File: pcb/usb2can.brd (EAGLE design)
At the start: 160 x 100 mm, 18 parts, among them IC1 ADM3053M, IC2 LD117AS33TR, K1 61400416021, K2 61900419521

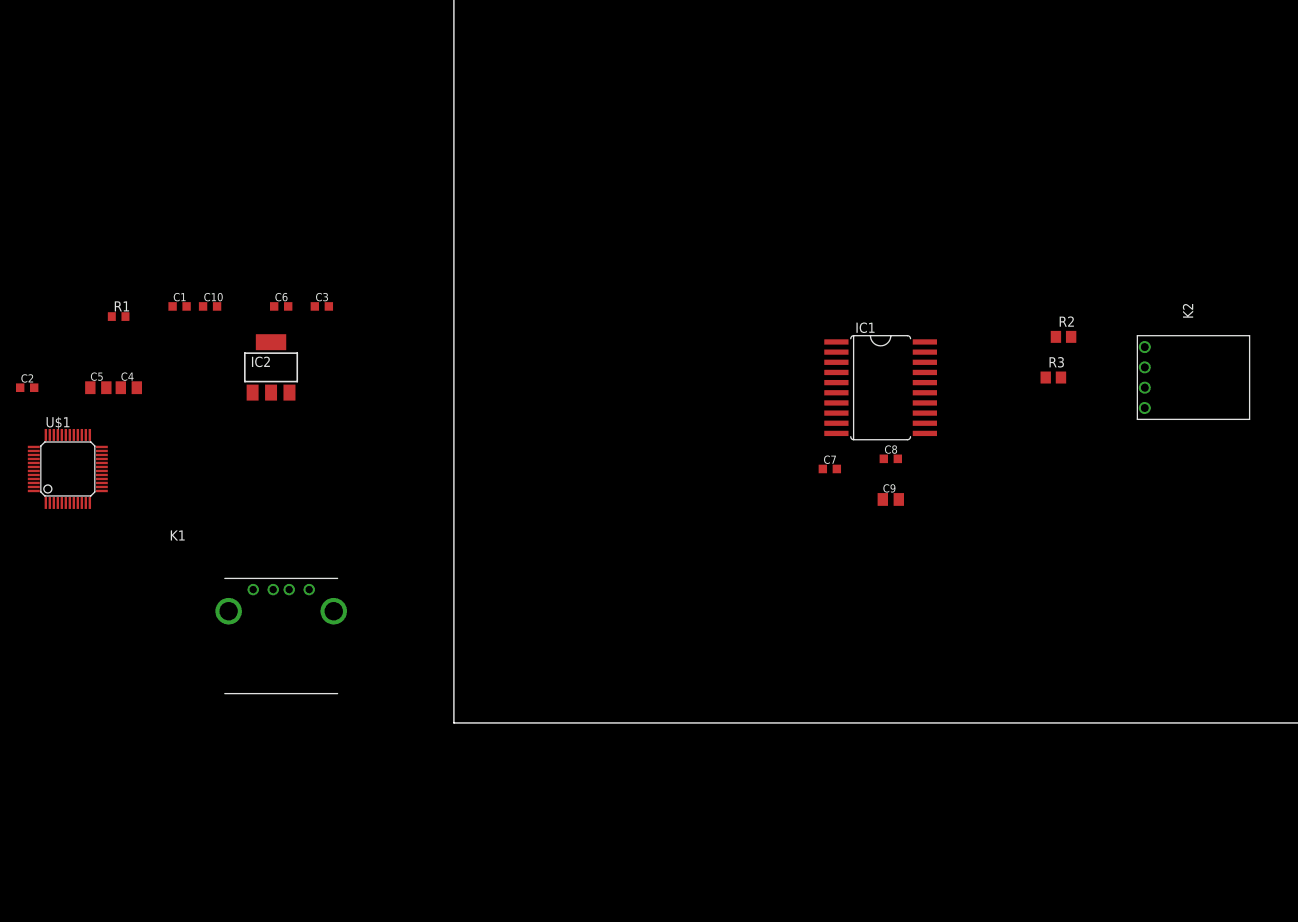
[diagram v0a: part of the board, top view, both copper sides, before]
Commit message: add some capacitors and connect USB and CAN
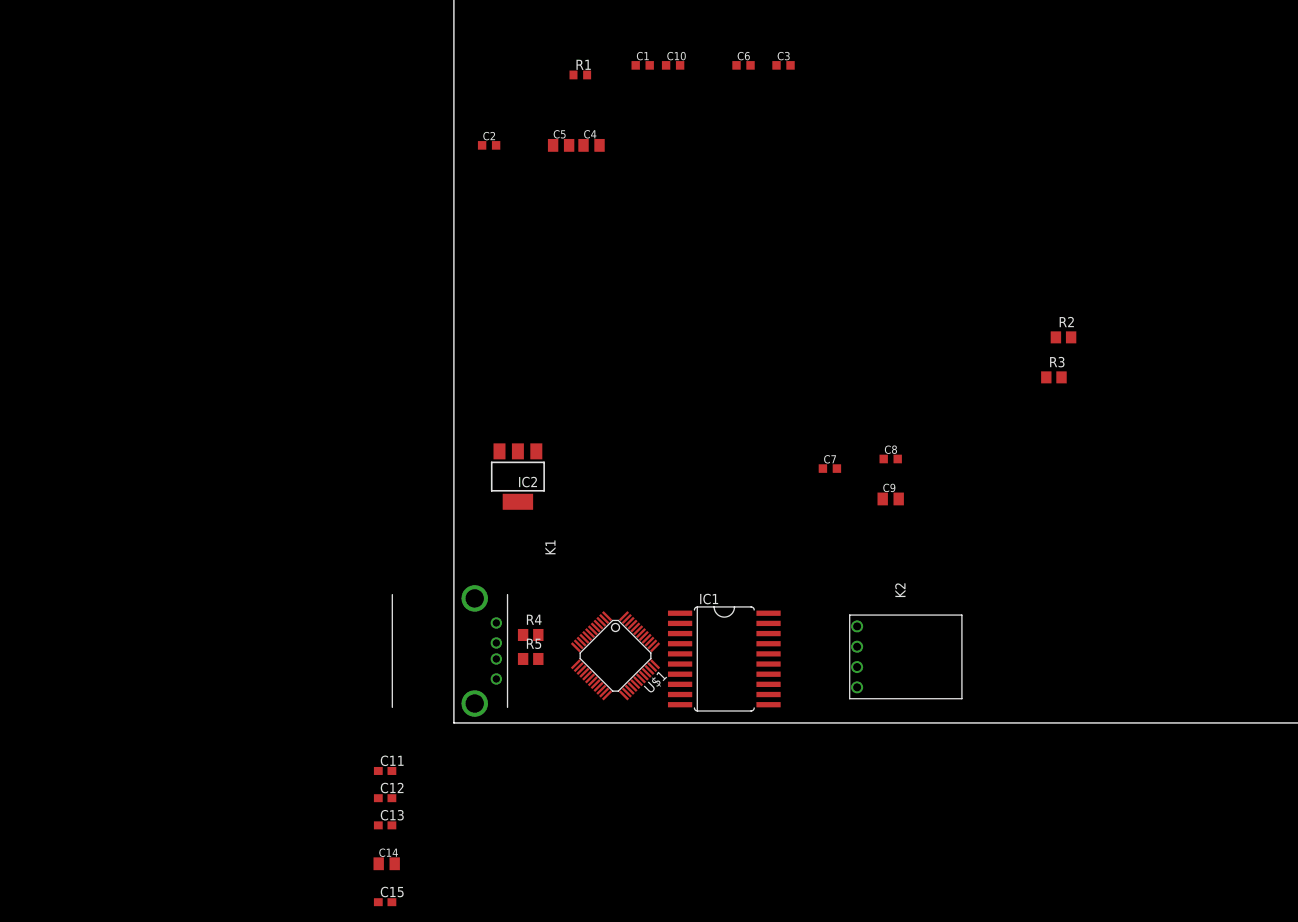
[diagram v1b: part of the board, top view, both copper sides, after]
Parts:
- added C11, C12, C13: 100n, rcl:C0603
- added C14: 10u, rcl:C0805K
- added C15: 10n, rcl:C0603
- added R4, R5: 22R, rcl:R0805
- moved U$1 72.3 mm to (20.2, 8.40), turned to 225 degrees
- moved C5 65.3 mm to (13.4, 72.2)
- moved C4 65.3 mm to (17.2, 72.2)
- moved C1 65.3 mm to (23.6, 82.2)
- moved C10 65.3 mm to (27.4, 82.2)
- moved C2 65.2 mm to (4.40, 72.2)
- moved C6 65.2 mm to (36.2, 82.2)
- moved R1 65.1 mm to (15.8, 81.0)
- moved C3 65.1 mm to (41.2, 82.2)
- moved K2 50.1 mm to (50.4, 10.8)
- moved IC1 39.1 mm to (33.8, 8.00)
- moved IC2 33.7 mm to (8.00, 30.8), turned to 180 degrees
- moved K1 24.7 mm to (2.60, 9.00), turned to 270 degrees
- moved R3 0.07 mm to (75.0, 43.2)
- moved C9 0.06 mm to (54.6, 28.0)
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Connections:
- removed net VBAT: U$1.1
- removed net VDD: U$1.24, U$1.48
- removed net VDDA: U$1.9
- removed net VDDIO2: U$1.36
- removed net VSS: U$1.23, U$1.35, U$1.47
- removed net VSSA: U$1.8
- new net CAN_RX: U$1.45
- new net CAN_TX: U$1.46
- new net N$5: K1.2, R4.1
- new net N$6: K1.3, R5.1
- new net N$7: C13.1, U$1.36
- new net USB_DM: R4.2, U$1.32
- new net USB_DP: R5.2, U$1.33
- net +3V3: now also C11.1, C12.1, C14.1, C15.1, U$1.1, U$1.24, U$1.48, U$1.9
- net GND: now also C11.2, C12.2, C13.2, C14.2, C15.2, U$1.23, U$1.35, U$1.47, U$1.8

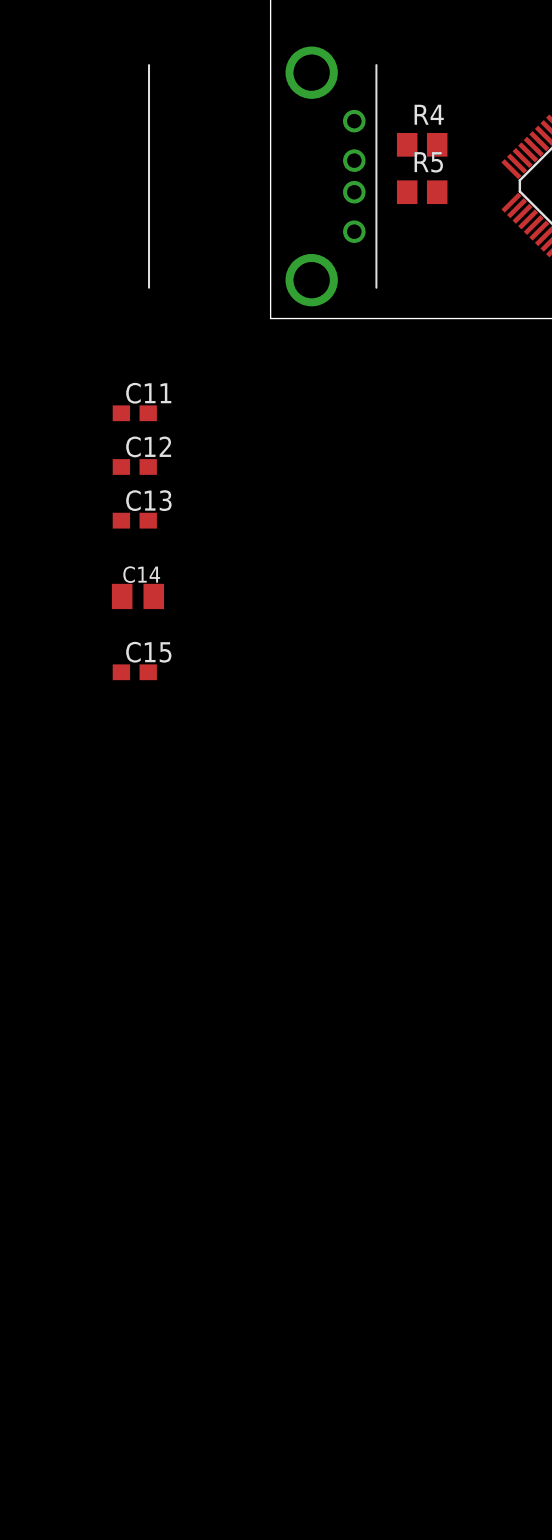
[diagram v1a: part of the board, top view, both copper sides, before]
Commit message: schematic: clock done, USB needs no series-R, debug port done, power supply revised
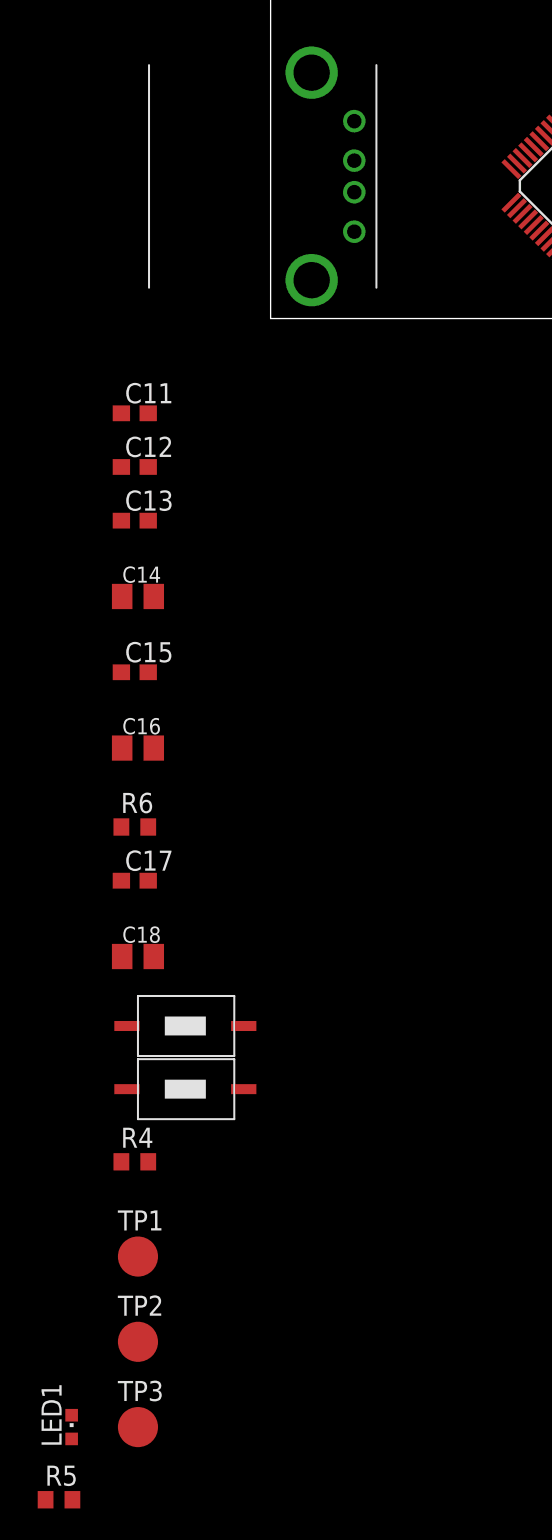
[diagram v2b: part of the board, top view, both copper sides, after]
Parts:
- added C16: 4.7u, rcl:C0805K
- added C17: 100n, rcl:C0603
- added C18: 1u, rcl:C0805K
- added LED1: GREEN, led:CHIPLED_0603
- added R6: 1k, resistor:R0603
- added S1, S2: MICRO_SWITCH_3X6X2.5S, micro_switch:MICRO_SWITCH_3X6X2.5
- added TP1, TP2, TP3: TPB2,54, testpad:B2,54
- C14: value 10u -> 4.7u
- R4: value 22R -> 510R; device rcl:R0805 -> resistor:R0603
- R5: value 22R -> 330R; device rcl:R0805 -> resistor:R0603
- moved R5 85.9 mm to (-13.4, -74.8)
- moved R4 66.9 mm to (-8.60, -53.4)
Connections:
- new net SWDCLK: TP1.TP, U$1.37
- new net SWDIO: TP2.TP, U$1.34
- net +3V3: now also C13.1, C16.1, C18.1, LED1.A, R6.1, S1.1, U$1.36
- net GND: now also C16.2, C17.2, C18.2, R4.1, R5.1, S2.1, TP3.TP, U$1.5
- net N$5: now also LED1.C, R5.2; no longer K1.2, R4.1
- net N$6: now also R4.2, S1.2, U$1.44; no longer K1.3, R5.1
- net N$7: now also C17.1, R6.2, S2.2, U$1.7; no longer C13.1, U$1.36
- net USB_DM: now also K1.2; no longer R4.2
- net USB_DP: now also K1.3; no longer R5.2

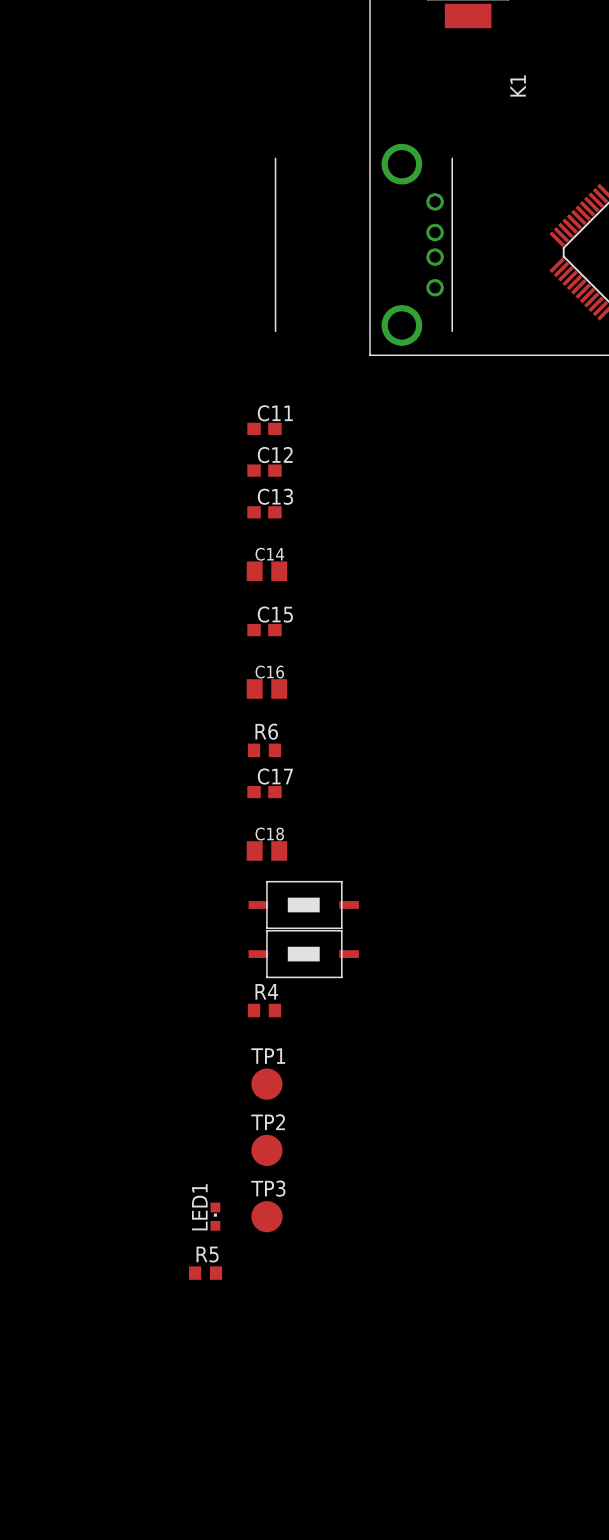
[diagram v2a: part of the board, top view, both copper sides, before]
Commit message: schematic: use another usb connector and add forgotten library
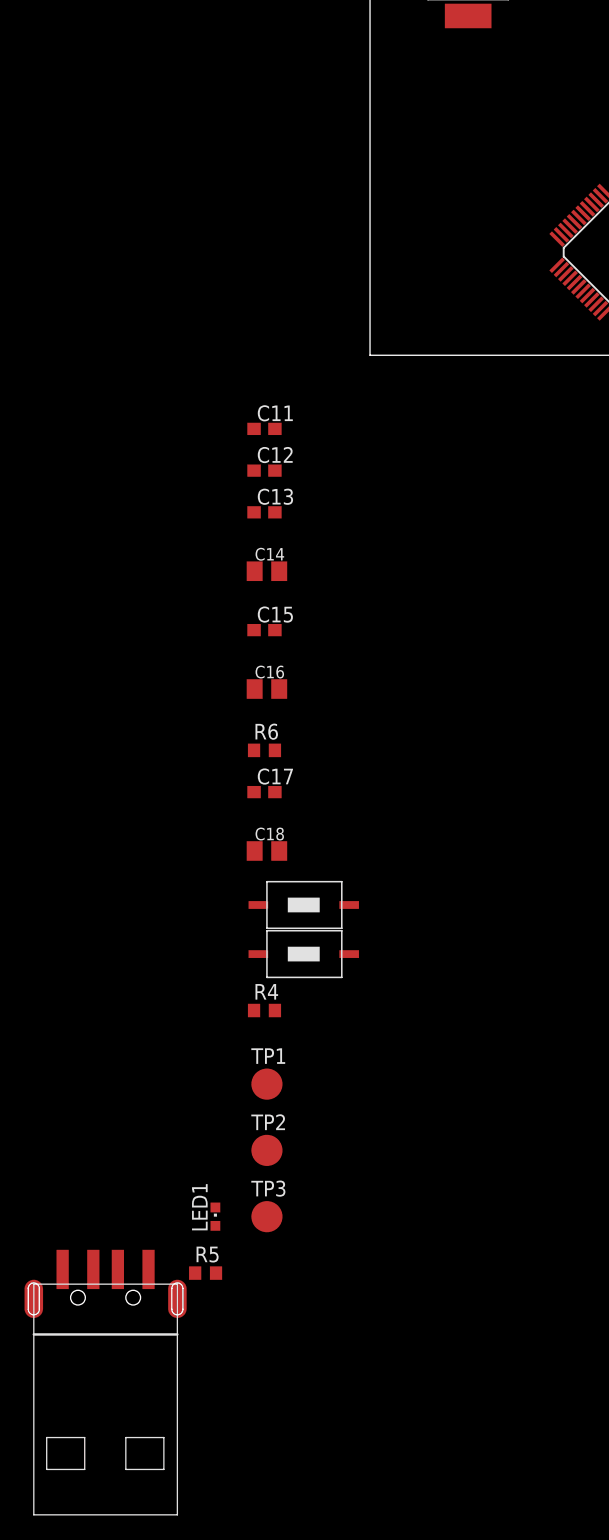
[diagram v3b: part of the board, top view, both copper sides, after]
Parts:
- removed K1: 61400416021, Wuerth_Elektronik_eiCan_Communication_Connectors:61400416021
- added CON1: USB_A_MALESMD, micro_switch:USB_A_MALE_SMD
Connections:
- net GND: now also CON1.4; no longer K1.4
- net USB_DM: now also CON1.2; no longer K1.2
- net USB_DP: now also CON1.3; no longer K1.3
- net VCC: now also CON1.1; no longer K1.1
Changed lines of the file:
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@@
 <elements>
 <element name="IC1" library="ADM3053" package="SO20W" value="ADM3053M" x="33.8" y="8" rot="R270"/>
-<element name="K1" library="Wuerth_Elektronik_eiCan_Communication_Connectors" package="61400416021" value="61400416021" x="2.6" y="9" rot="R270"/>
 <element name="C1" library="rcl" package="C0603K" value="10n" x="23.6" y="82.2"/>
 <element name="C2" library="rcl" package="C0603K" value="100n" x="4.4" y="72.2"/>
@@
 <element name="LED1" library="led" package="CHIPLED_0603" value="GREEN" x="-12.6" y="-70.2"/>
 <element name="R5" library="resistor" package="R0603" value="330R" x="-13.4" y="-74.8"/>
+<element name="CON1" library="micro_switch" package="USB_A_MALE_SMD" value="USB_A_MALESMD" x="-23.8" y="-76.8"/>
 </elements>
 <signals>
 <signal name="VCC">
-<contactref element="K1" pad="1"/>
 <contactref element="IC2" pad="3"/>
 <contactref element="C3" pad="1"/>
@@
 <contactref element="C5" pad="1"/>
 <contactref element="C6" pad="1"/>
+<contactref element="CON1" pad="1"/>
 <wire x1="35.325" y1="82.2" x2="40.325" y2="82.2" width="0" layer="19" extent="1-1"/>
 <wire x1="12.4" y1="72.2" x2="35.325" y2="82.2" width="0" layer="19" extent="1-1"/>
 <wire x1="5.7" y1="33.95" x2="12.4" y2="72.2" width="0" layer="19" extent="1-1"/>
-<wire x1="5.3" y1="12.5" x2="5.7" y2="33.95" width="0" layer="19" extent="1-1"/>
-<wire x1="28.2708" y1="4.825" x2="5.3" y2="12.5" width="0" layer="19" extent="1-1"/>
+<wire x1="28.2708" y1="4.825" x2="5.7" y2="33.95" width="0" layer="19" extent="1-1"/>
+<wire x1="-18.05" y1="-74.5" x2="28.2708" y2="4.825" width="0" layer="19" extent="1-1"/>
 </signal>
 <signal name="GND">
-<contactref element="K1" pad="4"/>
 <contactref element="C1" pad="2"/>
 <contactref element="C2" pad="2"/>
@@
 <contactref element="TP3" pad="TP"/>
 <contactref element="R5" pad="1"/>
+<contactref element="CON1" pad="4"/>
 <wire x1="37.075" y1="82.2" x2="42.075" y2="82.2" width="0" layer="19" extent="1-1"/>
 <wire x1="24.475" y1="82.2" x2="37.075" y2="82.2" width="0" layer="19" extent="1-1"/>
@@
 <wire x1="24.79619375" y1="6.985784375" x2="28.2708" y2="6.095" width="0" layer="19" extent="1-1"/>
 <wire x1="18.785784375" y1="3.803803125" x2="24.79619375" y2="6.985784375" width="0" layer="19" extent="1-1"/>
-<wire x1="5.3" y1="5.5" x2="16.664465625" y2="10.874871875" width="0" layer="19" extent="1-1"/>
-<wire x1="-7.75" y1="-6" x2="5.3" y2="5.5" width="0" layer="19" extent="1-1"/>
+<wire x1="-7.75" y1="-6" x2="18.785784375" y2="3.803803125" width="0" layer="19" extent="1-1"/>
 <wire x1="-7.75" y1="-9.4" x2="-7.75" y2="-6" width="0" layer="19" extent="1-1"/>
 <wire x1="-7.75" y1="-12.8" x2="-7.75" y2="-9.4" width="0" layer="19" extent="1-1"/>
@@
 <wire x1="-8.4" y1="-70.2" x2="-9.45" y2="-53.4" width="0" layer="19" extent="1-1"/>
 <wire x1="-14.25" y1="-74.8" x2="-8.4" y2="-70.2" width="0" layer="19" extent="1-1"/>
+<wire x1="-25.05" y1="-74.5" x2="-14.25" y2="-74.8" width="0" layer="19" extent="1-1"/>
 </signal>
 <signal name="CAN_TXD">
@@
 <signal name="USB_DM">
 <contactref element="U$1" pad="32"/>
-<contactref element="K1" pad="2"/>
-<wire x1="5.3" y1="10" x2="23.73553125" y2="5.925125" width="0" layer="19" extent="1-1"/>
+<contactref element="CON1" pad="2"/>
+<wire x1="23.73553125" y1="5.925125" x2="-20.55" y2="-74.5" width="0" layer="19" extent="1-1"/>
 </signal>
 <signal name="USB_DP">
 <contactref element="U$1" pad="33"/>
-<contactref element="K1" pad="3"/>
-<wire x1="5.3" y1="8" x2="24.089084375" y2="6.278678125" width="0" layer="19" extent="1-1"/>
+<contactref element="CON1" pad="3"/>
+<wire x1="24.089084375" y1="6.278678125" x2="-22.55" y2="-74.5" width="0" layer="19" extent="1-1"/>
 </signal>
 <signal name="CAN_RX">

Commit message: progress made by Martin
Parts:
- moved TP3 165.2 mm to (135.0, 11.8)
- moved TP2 157.7 mm to (135.2, 0.40)
- moved TP1 157.4 mm to (132.0, 11.8)
- moved R1 156.8 mm to (154.2, 7.40), flipped to the bottom, turned to 90 degrees
- moved CON1 154.7 mm to (105.8, 7.60), turned to 270 degrees
- moved C10 150.2 mm to (155.6, 4.00), flipped to the bottom
- moved R5 149.4 mm to (113.2, 4.60), flipped to the bottom
- moved LED1 148.8 mm to (111.2, 12.4), turned to 90 degrees
- moved R4 146.3 mm to (122.8, 11.0), flipped to the bottom, turned to 180 degrees
- moved S1 140.2 mm to (123.2, 11.0)
- moved C18 138.8 mm to (122.0, 7.20), flipped to the bottom, turned to 90 degrees
- moved C17 135.1 mm to (118.6, 9.80), flipped to the bottom, turned to 180 degrees
- moved C14 134.2 mm to (124.0, 4.00), flipped to the bottom, turned to 270 degrees
- moved C2 133.3 mm to (116.8, 0.60), turned to 90 degrees
- moved R6 132.2 mm to (117.6, 7.20), flipped to the bottom, turned to 90 degrees
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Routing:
- net GND: track 0.00 -> 126.5 mm, vias 0 -> 6
- net +3V3: track 0.00 -> 82.5 mm, vias 0 -> 8
- net GNDA: track 0.00 -> 44.1 mm, vias 0 -> 1
- net VCC: track 0.00 -> 39.1 mm, vias 0 -> 2
- net USB_DM: track 0.00 -> 32.7 mm, vias 0 -> 2
- net USB_DP: track 0.00 -> 32.1 mm, vias 0 -> 2
- net N$7: track 0.00 -> 24.8 mm, vias 0 -> 2
- net VISO: track 0.00 -> 19.4 mm, vias 0 -> 2
- net N$2: track 0.00 -> 14.6 mm
- net N$6: track 0.00 -> 11.6 mm, vias 0 -> 1
- net N$3: track 0.00 -> 10.8 mm
- net SWDCLK: track 0.00 -> 8.66 mm
- net N$5: track 0.00 -> 8.59 mm, vias 0 -> 1
- net N$4: track 0.00 -> 6.13 mm, vias 0 -> 2
- net N$1: track 0.00 -> 5.27 mm, vias 0 -> 1
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- added copper zone on layer 1, net GND
- added copper zone on layer 16, net GND
- added copper zone on layer 1, net GNDA
- added copper zone on layer 16, net GNDA
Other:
- board size 160 x 100 mm -> 57.8 x 17.2 mm
